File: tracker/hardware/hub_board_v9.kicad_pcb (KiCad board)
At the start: 4 copper layers, 103 x 103 mm, 39 parts, among them U1 ESP32-S3-WROOM-1U-N8R8, U2 LoRa2021F33-2G4, U3 LoRa2021_Castellated, U4 SX1280, U5 MAX-M10S, U6 MS5611-01BA, U7 TPS7A02

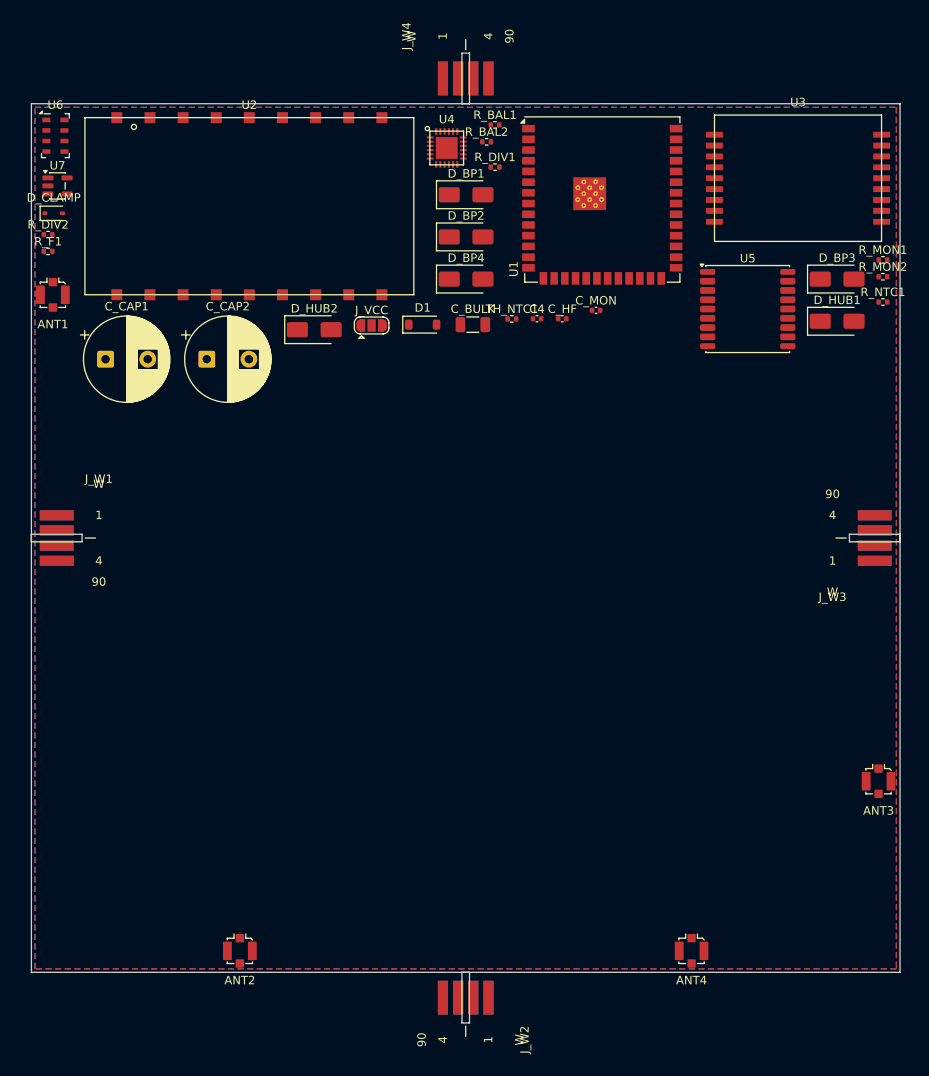
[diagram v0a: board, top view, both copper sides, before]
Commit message: fix(hub): STALE published board -- build's KRT_DIR was a path that does not exist; publish now REFUSES instead of silently no-oping
CLOSES THE OUTLINE FAIL IN MY OWN GATE, AND THE ROOT CAUSE WAS A REAL DEFECT, NOT A STALE FILE.

=== THE MEASURED DIAGNOSIS ===
The two hub boards disagreed on the outline:
    tracker/hardware/hub_board_v9.kicad_pcb (committed): Edge.Cuts 103.150 x 103.150 mm, 0 tracks
    docs/fab/hub-v9/gerbers/hub_v9.kicad_pcb (packaged): Edge.Cuts  70.150 x 70.150 mm, 537 tracks
Both carry the SAME 39 footprints. ADR-068 (revised 2026-10-14) sets the outline at 70 x 70, and
build_hub_board_v9.py is the SINGLE WRITER of the committed file with DEFAULT_W/H = 70.0. So the
committed file was STALE at the SUPERSEDED ADR-055 D5 103x103-class outline.

I ALSO CORRECTED MY OWN GATE, WHICH WAS WRONG: the check compared GetBoardEdgesBoundingBox(), which is
inflated by TRACK/VIA/COPPER extents, not just the outline. That is why it reported the packaged board
as 70.15 x 71.65 -- the extra 1.50 mm of height was COPPER reaching past the edge, NOT the board being
taller. A FALSE divergence FAIL against a board that was fine. The check now measures Edge.Cuts DRAWING
ITEMS ONLY, and reports 70.15 x 70.15 for both. (Both boards also carry a uniform 0.075 mm outset on
every side -- 103.075 - (-0.075) = 103.150 -- a drawing convention, so outline-to-outline is the
correct comparison, never nominal-against-measured.)

=== THE ROOT CAUSE: A PATH THAT DOES NOT EXIST, AND A RETURN CODE NOBODY CHECKED ===
KRT_DIR was hard-coded to ~/tools/KiCadRoutingTools, WHICH DOES NOT EXIST ON THIS HOST -- the real
checkout is ~/repos/KiCadRoutingTools -> /data/repos/KiCadRoutingTools. run_krt therefore took its
"placer absent" branch, printed a note, and returned 1 -- AND main() DISCARDED THE RETURN CODE, so
--publish reported success while leaving the STALE committed board in place. That is exactly how the
103.15 x 103.15 outline survived: the publish never happened and nothing said 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
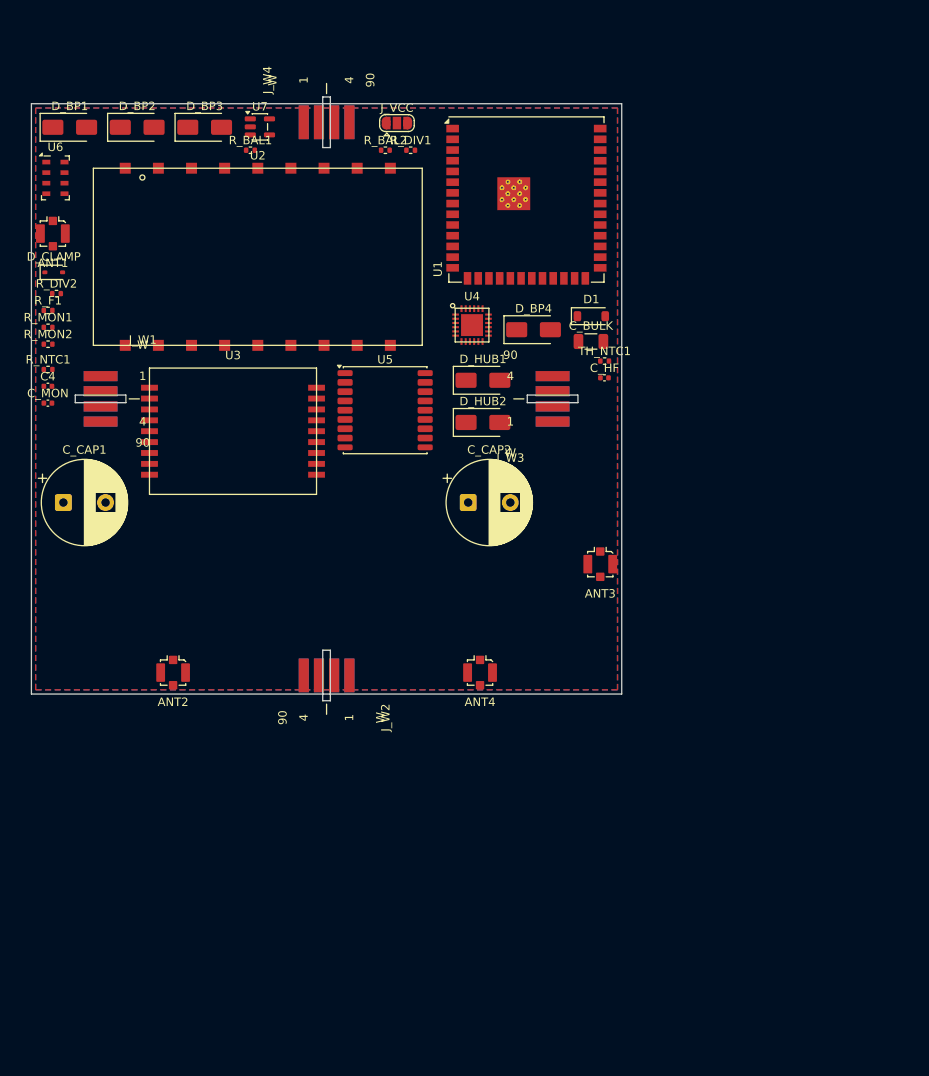
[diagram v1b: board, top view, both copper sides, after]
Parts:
- moved R_MON1 99.3 mm to (1.98, 26.5)
- moved R_MON2 99.3 mm to (1.98, 28.5)
- moved R_NTC1 99.3 mm to (1.98, 31.5)
- moved D_BP3 77.1 mm to (20.5, 2.79)
- moved U3 73.4 mm to (23.9, 38.8)
- moved C_MON 65.9 mm to (1.96, 35.5)
- moved C4 58.5 mm to (1.96, 33.5)
- moved D_BP1 47.7 mm to (4.54, 2.79)
- moved U5 44.6 mm to (41.9, 36.3)
- moved D_HUB1 42.6 mm to (53.5, 32.8)
- moved ANT3 41.9 mm to (67.5, 54.6)
- moved J_W2 41.6 mm to (35.0, 64.8)
- moved J_W3 41.6 mm to (64.8, 35.0)
- moved ANT4 41.4 mm to (53.2, 67.5)
- moved D_BP2 41.1 mm to (12.5, 2.79)
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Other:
- board size 103 x 103 mm -> 70 x 70 mm

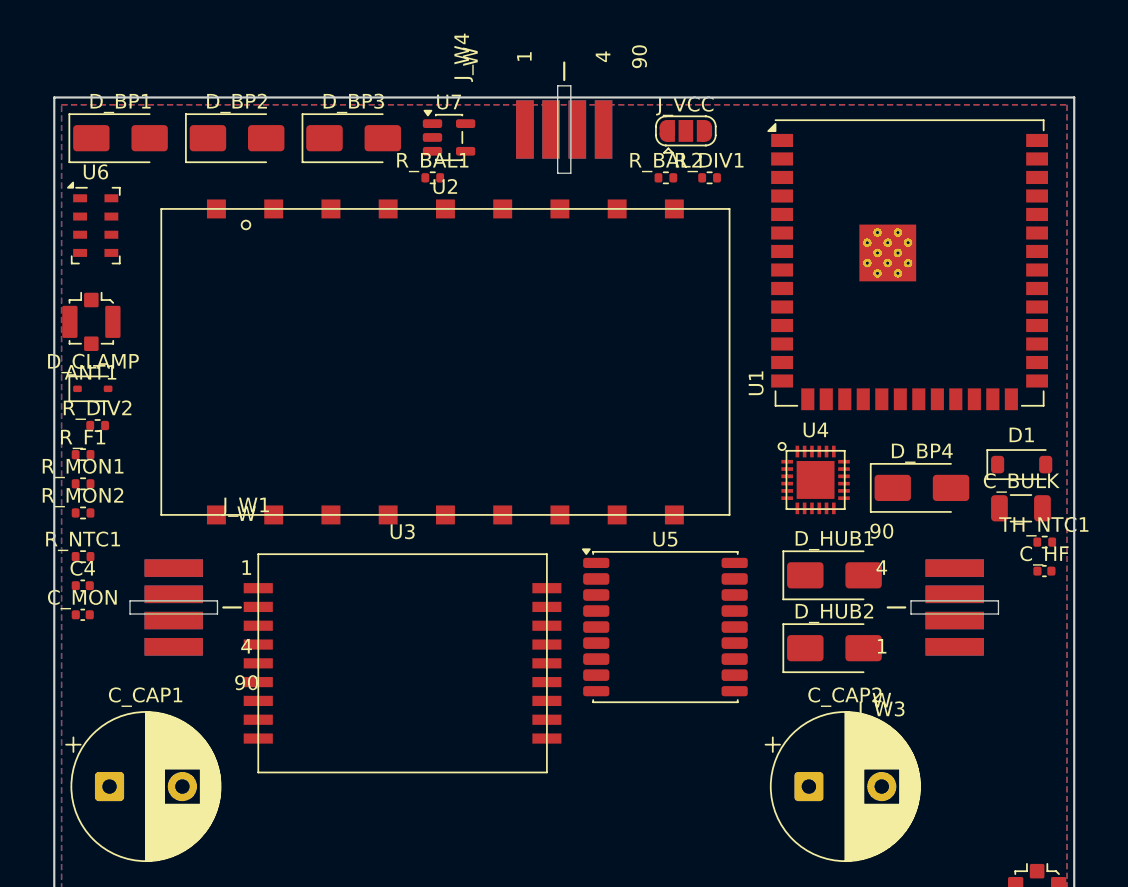
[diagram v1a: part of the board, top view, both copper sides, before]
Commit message: feat(hub): 44/44 PLACED -- the 7-missing-parts defect is CLOSED at the board level; gate now names the stale package
THE DEFECT THAT REACHED THE ORDER PACKAGE IS FIXED. Rebuilt with --publish after the symbol surgery:
    components : 44 on netlist / 44 placed / 0 with an EMPTY footprint field   (was 46/39/7)
    outline    : 70.0 x 70.0 mm
    krt placer : parts_moved 17, pad_overlap_pairs 0, pad_intersection_pairs 0
    frozen board: tracker/hardware/hub_board_v9.kicad_pcb  sha256 c0ff66dc...
U_CUT1-4 (SN74LVC1G373DBVR, SOT-23-6) and U_HUB_CVT (BQ25504RGTR, VQFN-16) are now physically placed.
PVA1/PVA2 correctly left the board.

I ALSO FIXED A CONFLATION IN MY OWN GATE THAT WAS HIDING WHICH LINK WAS BROKEN.
Section C compared the netlist against the PACKAGED board only, so when the committed board had been
regenerated to 44/44 while the packaged (routed) artifact still carried 39, it reported ONE opaque
failure. There are two distinct links and they are now checked separately:
    C1  netlist  ->  the single-writer's COMMITTED board   (is the design placed at all?)
    C2  committed ->  the PACKAGED board                   (is the order package current?)
RESULT: C1 PASSES (netlist declares 44, committed board carries 44). C2 FAILS CORRECTLY, naming the
exact staleness: "the packaged board is STALE: it lacks ['U_CUT1','U_CUT2','U_CUT3','U_CUT4',
'U_HUB_CVT']" and saying to route the committed board, re-emit BOM/CPL/gerbers, and copy it into the
package. A check that names the broken link is worth more than one that reports a symptom.

GATE: test_netlist_integrity.py 14 pass, 1 FAIL -- and the one failure is a REAL, ACTIONABLE state,
not a defect in the design. Sections A (empty footprint) and B (unresolvable footprint) PASS, and C1
PASSES. test_order_package_consistency.py remains 5 pass / 1 FAIL (the three-slot gap, awaiting Site C).

WHAT REMAINS FOR THE HUB ORDER PACKAGE: route the committed 44-part board, then re-emit the BOM and
CPL and the gerbers and copy th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
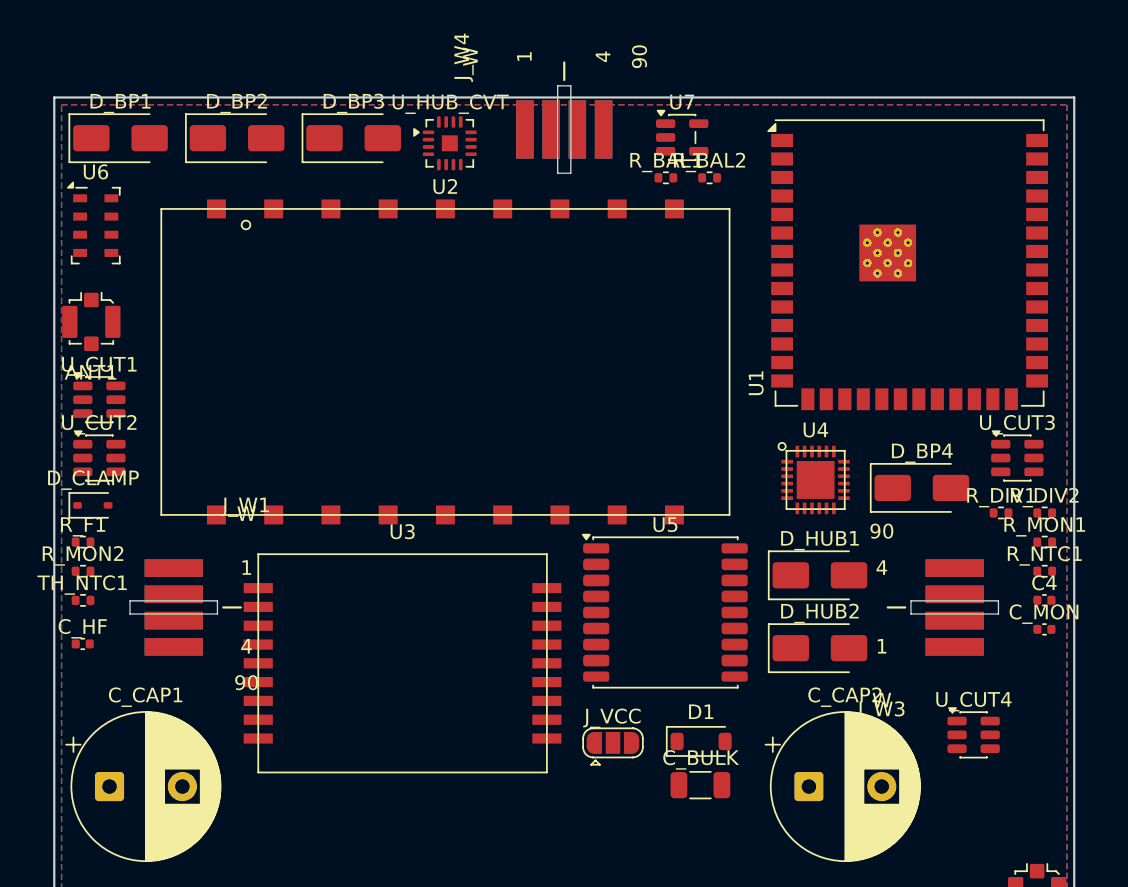
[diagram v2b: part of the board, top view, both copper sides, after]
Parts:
- added U_CUT1: SN74LVC1G373DBVR, Package_TO_SOT_SMD:SOT-23-6, F.Cu at (3.10, 20.7)
- added U_CUT2: SN74LVC1G373DBVR, Package_TO_SOT_SMD:SOT-23-6, F.Cu at (3.10, 24.7)
- added U_CUT3: SN74LVC1G373DBVR, Package_TO_SOT_SMD:SOT-23-6, F.Cu at (66.1, 24.7)
- added U_CUT4: SN74LVC1G373DBVR, Package_TO_SOT_SMD:SOT-23-6, F.Cu at (63.1, 43.7)
- added U_HUB_CVT: BQ25504RGTR, Package_DFN_QFN:VQFN-16-1EP_3x3mm_P0.5mm_EP1.1x1.1mm, F.Cu at (27.1, 3.15)
- moved C_HF 66.2 mm to (1.96, 37.5)
- moved R_MON1 66.1 mm to (68.0, 30.5)
- moved TH_NTC1 66.1 mm to (1.98, 34.5)
- moved C4 66.0 mm to (68.0, 34.5)
- moved C_MON 66.0 mm to (68.0, 36.5)
- moved R_NTC1 66.0 mm to (68.0, 32.5)
- moved R_DIV2 65.3 mm to (68.0, 28.5)
- moved J_VCC 42.3 mm to (38.3, 44.3)
- moved R_DIV1 30.5 mm to (65.0, 28.5)
- moved C_BULK 29.1 mm to (44.3, 47.2)
- moved D1 29.1 mm to (44.4, 44.2)
- moved R_BAL1 16.0 mm to (42.0, 5.51)
- moved U7 16.0 mm to (43.1, 2.75)
- moved D_CLAMP 8.00 mm to (2.65, 28.0)
- moved R_F1 6.00 mm to (1.98, 30.5)
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
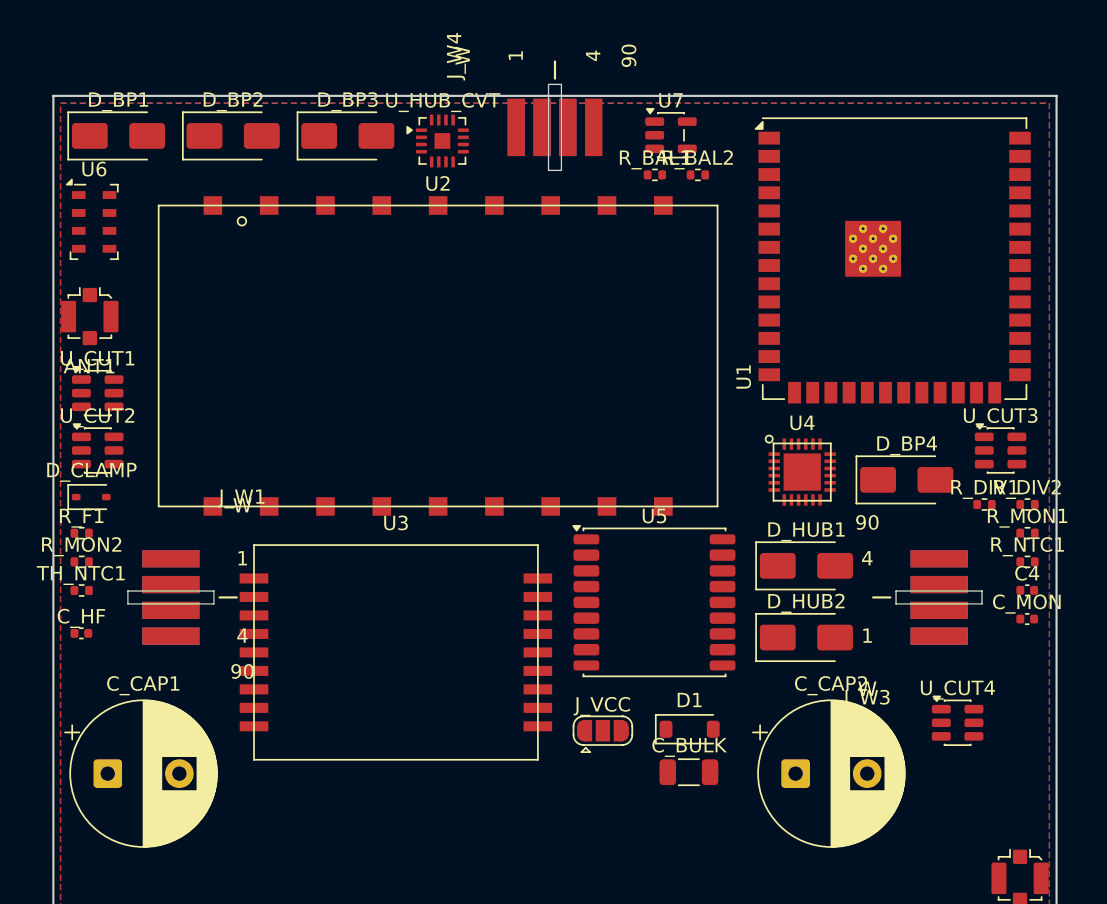
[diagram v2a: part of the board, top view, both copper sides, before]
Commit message: fix(hub): place all 15 U4 support/RF parts on the board -- CLEARS THE ORDER BLOCKER
`test_netlist_integrity.py` section C was THE ORDER BLOCKER:

    FAIL  C. v9 hub board carries every netlist component
          MISSING FROM THE BOARD (15): ['C0','C1','C10','C2','C3','C5','C6','C7','C8','C9',
                                        'L1','L2','L4','Q1','R15']
          THIS IS THE ORDER BLOCKER.

Those are exactly the parts the U4 (SX1280) rewire added to the schematic. The board could not
carry them, so the delivered hardware could not perform those functions regardless of firmware.

THE FIX WAS A RE-RUN, NOT A HAND-EDIT. `build_hub_board_v9.py` is the SINGLE WRITER of
`hub_board_v9.kicad_pcb` (placement_guard.py R1) with NO hand-typed coordinate table (R2): every
position is a netlist fact, a library footprint's own measured geometry, or a COMPUTED parametric
seat over the outline. It places EVERY netlist component whose library resolves. Measured:

    components : 59 on netlist / 59 placed / 0 with an EMPTY footprint field
    outline    : 70.0 x 70.0 mm (4-layer, 0.6 mm)
    edge-seated: J_W1..J_W4, ANT1..ANT4
    seed       : output/hub_board_v9_seed.kicad_pcb  sha256 3a2e3163...  (gitignored intermediate)
    krt lap    : EXIT=0, parts_moved 29
    frozen     : hub_board_v9.kicad_pcb  sha256 ce196e65...  (+10,835 / -8,606 lines)
    board now  : 59 footprints, the 15 U4 parts 15/15 present

All 15 use STOCK KiCad libraries (Capacitor_SMD 0402, Inductor_SMD 0402/1210,
Crystal_SMD_3225-4Pin, Resistor_SMD 0402), so no library work was needed. Q1 is a 4-pin
`Crystal_SMD_3225-4Pin_3.2x2.5mm`, consistent with the delegated worker's independent finding that
the part is a Crystal_GND24-style land (pads 1 and 3 electrodes, 2 and 4 ground).

GATE RESULT: 9 pass / 7 FAIL  ->  12 pass / 4 FAIL
    PASS  C.  v9 hub: board carries every netlist component        <-- WAS THE ORDER BLOCKER
    PASS  C.  v9 hub: no extra footprints the netlist does not declare

!!! A REVERTED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
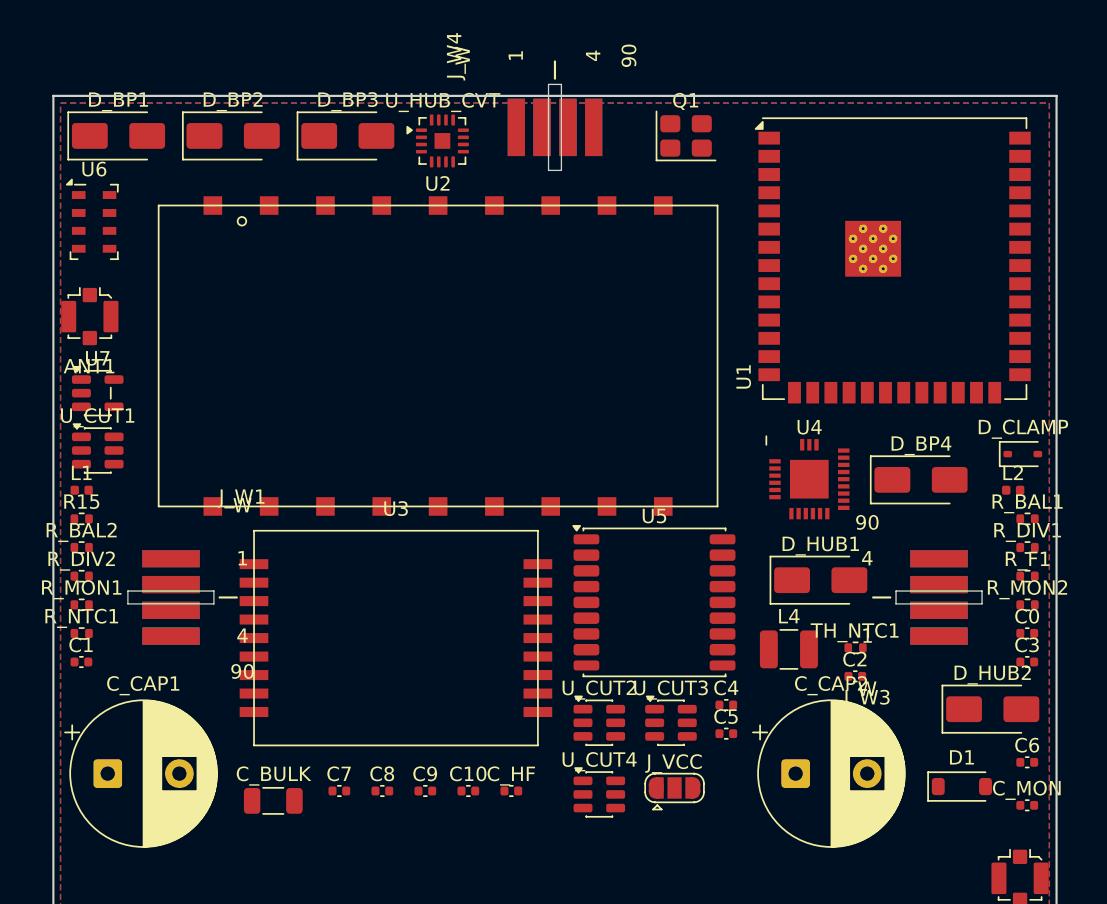
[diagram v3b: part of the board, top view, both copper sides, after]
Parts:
- added C0: 0.8pF, Capacitor_SMD:C_0402_1005Metric, F.Cu at (68.0, 37.5)
- added C1: 1.2pF, Capacitor_SMD:C_0402_1005Metric, F.Cu at (1.96, 39.5)
- added C10: 100nF, Capacitor_SMD:C_0402_1005Metric, F.Cu at (29.0, 48.5)
- added C2: 1.2pF, Capacitor_SMD:C_0402_1005Metric, F.Cu at (56.0, 40.5)
- added C3: 100pF, Capacitor_SMD:C_0402_1005Metric, F.Cu at (68.0, 39.5)
- added C5: 10nF, Capacitor_SMD:C_0402_1005Metric, F.Cu at (47.0, 44.5)
- added C6: 10nF, Capacitor_SMD:C_0402_1005Metric, F.Cu at (68.0, 46.5)
- added C7: 0.5pF, Capacitor_SMD:C_0402_1005Metric, F.Cu at (20.0, 48.5)
- added C8: 100nF, Capacitor_SMD:C_0402_1005Metric, F.Cu at (23.0, 48.5)
- added C9: 470nF, Capacitor_SMD:C_0402_1005Metric, F.Cu at (26.0, 48.5)
- added L1: 3.0nH, Inductor_SMD:L_0402_1005Metric, F.Cu at (1.98, 27.5)
- added L2: 2.5nH, Inductor_SMD:L_0402_1005Metric, F.Cu at (67.0, 27.5)
- added L4: 15uH, Inductor_SMD:L_1210_3225Metric, F.Cu at (51.3, 38.6)
- added Q1: 52MHz, Crystal:Crystal_SMD_3225-4Pin_3.2x2.5mm, F.Cu at (44.1, 2.79)
- added R15: 0R, Resistor_SMD:R_0402_1005Metric, F.Cu at (1.98, 29.5)
- moved R_DIV2 66.2 mm to (1.98, 33.5)
- moved R_MON1 66.2 mm to (1.98, 35.5)
- moved R_NTC1 66.2 mm to (1.98, 37.5)
- moved R_F1 66.1 mm to (68.0, 33.5)
- moved R_MON2 66.1 mm to (68.0, 35.5)
- moved D_CLAMP 65.1 mm to (67.6, 25.0)
- moved TH_NTC1 54.1 mm to (56.0, 38.5)
- moved R_BAL2 50.2 mm to (1.98, 31.5)
- moved U7 43.9 mm to (3.10, 20.7)
- moved U_CUT2 39.8 mm to (38.1, 43.7)
- moved R_BAL1 35.4 mm to (68.0, 29.5)
- moved C_HF 32.0 mm to (32.0, 48.5)
- moved U_CUT3 29.8 mm to (43.1, 43.7)
- moved C_BULK 29.1 mm to (15.3, 49.2)
- moved U_CUT4 25.5 mm to (38.1, 48.7)
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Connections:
- U1 pad 35: /SX1280_ANT_SW -> (no net)
- U4 pad 1: +3V3 -> /SX1280_VR_PA
- U4 pad 10: /SX1280_DIO1 -> /SX1280_DIO3
- U4 pad 11: /SX1280_DIO2 -> /SX1280_VBAT_IO
- U4 pad 12: /SX1280_DIO3 -> /SX1280_VDD
- U4 pad 13: /SX1280_ANT_SW -> GND
- U4 pad 14: /ANT2_2G4_RANGE -> /SX1280_DCC_SW
- U4 pad 15: GND -> +3V3
- U4 pad 16: GND -> /SX1280_MISO
- U4 pad 17: GND -> /SX1280_MOSI
- U4 pad 18: GND -> /SX1280_SCK
- U4 pad 19: GND -> /SX1280_CS_N
- U4 pad 2: +3V3 -> /SX1280_VDD
- U4 pad 22: GND -> /SX1280_RF
- U4 pad 25: GND -> (no net)
- U4 pad 3: GND -> /SX1280_RESET_N
- U4 pad 4: /SX1280_RESET_N -> /SX1280_XTA
- U4 pad 5: /SX1280_BUSY -> GND
- U4 pad 6: /SX1280_CS_N -> /SX1280_XTB
- U4 pad 7: /SX1280_SCK -> /SX1280_BUSY
- U4 pad 8: /SX1280_MOSI -> /SX1280_DIO1
- U4 pad 9: /SX1280_MISO -> /SX1280_DIO2
